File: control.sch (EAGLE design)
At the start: 11 parts, among them J1 1-2328702-0, U2 ESP32-DEVKITC-32D

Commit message: Found wurth typec
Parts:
- added J2: 12401598E4#2A, 12401598E4_2A:12401598E4#2A
- added R1, R2: 2k2, rcl:R-EU_R0805
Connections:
- new net RST: U$1.RST, U2.IO17
- net 3V3: now also R1.2, R2.2
- net SCL: now also R2.1
- net SDA: now also R1.1
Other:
- moved on the sheet: BT2
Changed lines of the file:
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@@
 <part name="C4" library="rcl" library_urn="urn:adsk.eagle:library:334" deviceset="C-EU" device="C1210" package3d_urn="urn:adsk.eagle:package:23619/2" value="100u"/>
 <part name="C5" library="rcl" library_urn="urn:adsk.eagle:library:334" deviceset="C-EU" device="C1210" package3d_urn="urn:adsk.eagle:package:23619/2" value="100u"/>
+<part name="R1" library="rcl" library_urn="urn:adsk.eagle:library:334" deviceset="R-EU_" device="R0805" package3d_urn="urn:adsk.eagle:package:23553/2" value="2k2"/>
+<part name="R2" library="rcl" library_urn="urn:adsk.eagle:library:334" deviceset="R-EU_" device="R0805" package3d_urn="urn:adsk.eagle:package:23553/2" value="2k2"/>
+<part name="J2" library="12401598E4_2A" deviceset="12401598E4#2A" device=""/>
 </parts>
 <sheets>
@@
 <attribute name="VALUE" x="177.8" y="104.14" size="1.778" layer="96"/>
 </instance>
-<instance part="BT2" gate="G$1" x="281.94" y="116.84" smashed="yes" rot="R270">
-<attribute name="NAME" x="285.75" y="120.65" size="1.778" layer="95" rot="R270"/>
-<attribute name="VALUE" x="276.86" y="120.65" size="1.778" layer="96" rot="R270"/>
+<instance part="BT2" gate="G$1" x="281.94" y="114.3" smashed="yes" rot="R270">
+<attribute name="NAME" x="285.75" y="118.11" size="1.778" layer="95" rot="R270"/>
+<attribute name="VALUE" x="276.86" y="118.11" size="1.778" layer="96" rot="R270"/>
 </instance>
 <instance part="C1" gate="G$1" x="215.9" y="121.92" smashed="yes">
@@
 <attribute name="NAME" x="245.364" y="99.441" size="1.778" layer="95"/>
 <attribute name="VALUE" x="245.364" y="94.361" size="1.778" layer="96"/>
+</instance>
+<instance part="R1" gate="G$1" x="284.48" y="137.16" smashed="yes" rot="R90">
+<attribute name="NAME" x="282.9814" y="133.35" size="1.778" layer="95" rot="R90"/>
+<attribute name="VALUE" x="287.782" y="133.35" size="1.778" layer="96" rot="R90"/>
+</instance>
+<instance part="R2" gate="G$1" x="276.86" y="137.16" smashed="yes" rot="R90">
+<attribute name="NAME" x="275.3614" y="133.35" size="1.778" layer="95" rot="R90"/>
+<attribute name="VALUE" x="280.162" y="133.35" size="1.778" layer="96" rot="R90"/>
+</instance>
+<instance part="J2" gate="G$1" x="309.88" y="88.9" smashed="yes">
+<attribute name="NAME" x="302.248009375" y="124.512" size="2.54" layer="95"/>
+<attribute name="VALUE" x="302.24645" y="50.7368" size="2.54" layer="96"/>
 </instance>
 </instances>
@@
 <junction x="261.62" y="116.84"/>
 <pinref part="BT2" gate="G$1" pin="NEG"/>
-<wire x1="261.62" y1="109.22" x2="281.94" y2="109.22" width="0.1524" layer="91"/>
 <junction x="261.62" y="109.22"/>
 <wire x1="246.38" y1="116.84" x2="261.62" y2="116.84" width="0.1524" layer="91"/>
 <junction x="246.38" y="116.84"/>
 <wire x1="215.9" y1="116.84" x2="228.6" y2="116.84" width="0.1524" layer="91"/>
+<wire x1="261.62" y1="109.22" x2="261.62" y2="106.68" width="0.1524" layer="91"/>
+<wire x1="261.62" y1="106.68" x2="281.94" y2="106.68" width="0.1524" layer="91"/>
 </segment>
 <segment>
@@
 <label x="215.9" y="124.46" size="1.778" layer="95"/>
 <pinref part="U$1" gate="G$1" pin="VCC"/>
+<wire x1="215.9" y1="124.46" x2="215.9" y2="142.24" width="0.1524" layer="91"/>
+<junction x="215.9" y="124.46"/>
+<pinref part="R1" gate="G$1" pin="2"/>
+<wire x1="215.9" y1="142.24" x2="276.86" y2="142.24" width="0.1524" layer="91"/>
+<pinref part="R2" gate="G$1" pin="2"/>
+<wire x1="276.86" y1="142.24" x2="284.48" y2="142.24" width="0.1524" layer="91"/>
+<junction x="276.86" y="142.24"/>
 </segment>
 </net>
@@
 <segment>
 <pinref part="U$1" gate="G$1" pin="SCL@1"/>
-<wire x1="261.62" y1="132.08" x2="271.78" y2="132.08" width="0.1524" layer="91"/>
+<wire x1="261.62" y1="132.08" x2="276.86" y2="132.08" width="0.1524" layer="91"/>
 <label x="266.7" y="132.08" size="1.778" layer="95"/>
+<pinref part="R2" gate="G$1" pin="1"/>
 </segment>
 <segment>
@@
 <segment>
 <pinref part="U$1" gate="G$1" pin="SDA"/>
-<wire x1="261.62" y1="124.46" x2="271.78" y2="124.46" width="0.1524" layer="91"/>
+<wire x1="261.62" y1="124.46" x2="284.48" y2="124.46" width="0.1524" layer="91"/>
 <label x="266.7" y="124.46" size="1.778" layer="95"/>
+<wire x1="284.48" y1="124.46" x2="284.48" y2="132.08" width="0.1524" layer="91"/>
+<pinref part="R1" gate="G$1" pin="1"/>
 </segment>
 <segment>
@@
 <segment>
 <pinref part="U$1" gate="G$1" pin="VBAT"/>
-<wire x1="261.62" y1="121.92" x2="276.86" y2="121.92" width="0.1524" layer="91"/>
+<wire x1="261.62" y1="121.92" x2="281.94" y2="121.92" width="0.1524" layer="91"/>
 <pinref part="BT2" gate="G$1" pin="POS"/>
-<label x="279.4" y="124.46" size="1.778" layer="95"/>
-<wire x1="281.94" y1="124.46" x2="276.86" y2="124.46" width="0.1524" layer="91"/>
-<wire x1="276.86" y1="124.46" x2="276.86" y2="121.92" width="0.1524" layer="91"/>
+<label x="279.4" y="121.92" size="1.778" layer="95"/>
 </segment>
 </net>
@@
 <label x="213.36" y="55.88" size="1.778" layer="95"/>
 <pinref part="U2" gate="G$1" pin="IO0"/>
+</segment>
+</net>
+<net name="RST" class="0">
+<segment>
+<pinref part="U$1" gate="G$1" pin="RST"/>
+<wire x1="220.98" y1="119.38" x2="228.6" y2="119.38" width="0.1524" layer="91"/>
+<label x="220.98" y="119.38" size="1.778" layer="95"/>
+</segment>
+<segment>
+<wire x1="213.36" y1="63.5" x2="220.98" y2="63.5" width="0.1524" layer="91"/>
+<label x="213.36" y="63.5" size="1.778" layer="95"/>
+<pinref part="U2" gate="G$1" pin="IO17"/>
 </segment>
 </net>
@@
 packages will not be understood (or retained) with this version.
 </note>
+<note version="8.4" severity="warning">
+Since Version 8.4, EAGLE supports properties for SPICE simulation.
+Probes in schematics and SPICE mapping objects found in parts and library devices
+will not be understood with this version. Update EAGLE to the latest version
+for full support of SPICE simulation.
+</note>
 </compatibility>

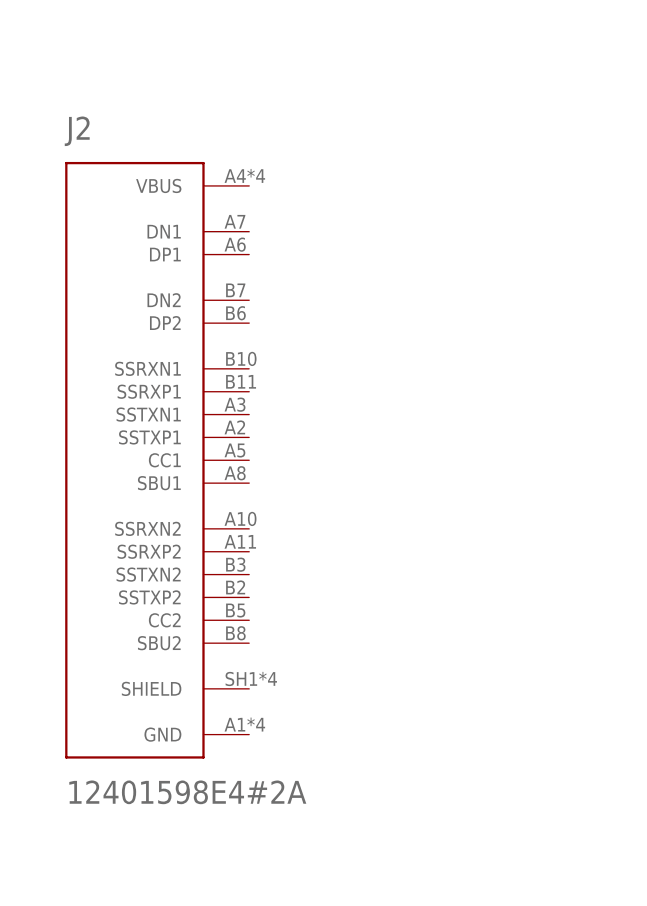
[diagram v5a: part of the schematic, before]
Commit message: started ratsnest, finished usb-c viring
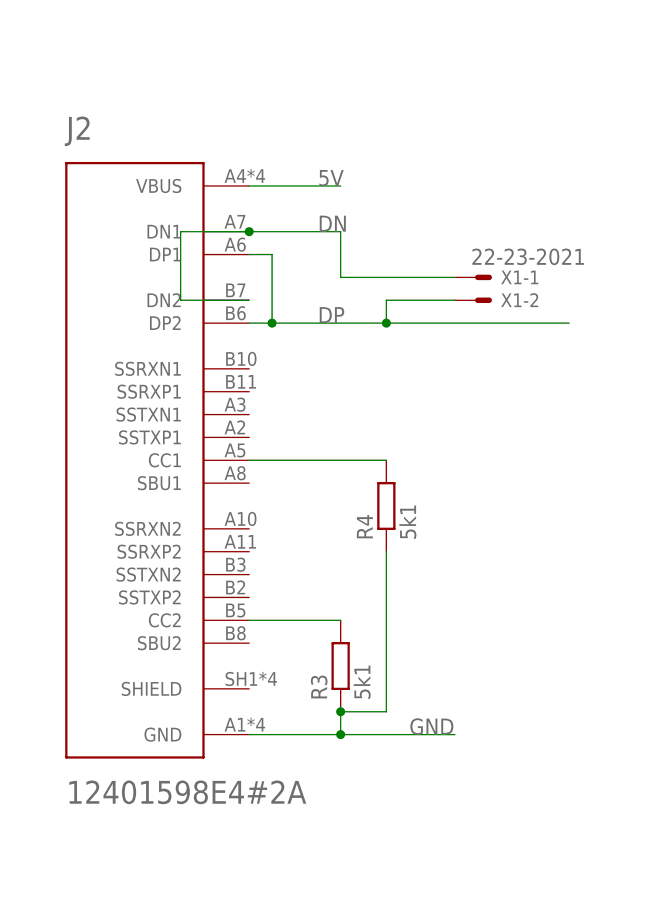
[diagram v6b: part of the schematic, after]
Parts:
- added R3, R4: 5k1, rcl:R-EU_R0805
- added X1: 22-23-2021, con-molex:22-23-2021
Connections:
- new net DN: J2.DN1, J2.DN2, X1-1.S
- new net DP: J2.DP1, J2.DP2, X1-2.S
- new net N$1: J2.CC2, R3.2
- new net N$2: J2.CC1, R4.2
- net 5V: now also J2.VBUS
- net GND: now also J2.GND, R3.1, R4.1
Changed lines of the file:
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@@
 <part name="R2" library="rcl" library_urn="urn:adsk.eagle:library:334" deviceset="R-EU_" device="R0805" package3d_urn="urn:adsk.eagle:package:23553/2" value="2k2"/>
 <part name="J2" library="12401598E4_2A" deviceset="12401598E4#2A" device=""/>
+<part name="R3" library="rcl" library_urn="urn:adsk.eagle:library:334" deviceset="R-EU_" device="R0805" package3d_urn="urn:adsk.eagle:package:23553/2" value="5k1"/>
+<part name="R4" library="rcl" library_urn="urn:adsk.eagle:library:334" deviceset="R-EU_" device="R0805" package3d_urn="urn:adsk.eagle:package:23553/2" value="5k1"/>
+<part name="X1" library="con-molex" library_urn="urn:adsk.eagle:library:165" deviceset="22-23-2021" device="" package3d_urn="urn:adsk.eagle:package:8078633/1"/>
 </parts>
 <sheets>
@@
 <attribute name="VALUE" x="302.24645" y="50.7368" size="2.54" layer="96"/>
 </instance>
+<instance part="R3" gate="G$1" x="332.74" y="66.04" smashed="yes" rot="R90">
+<attribute name="NAME" x="331.2414" y="62.23" size="1.778" layer="95" rot="R90"/>
+<attribute name="VALUE" x="336.042" y="62.23" size="1.778" layer="96" rot="R90"/>
+</instance>
+<instance part="R4" gate="G$1" x="337.82" y="83.82" smashed="yes" rot="R90">
+<attribute name="NAME" x="336.3214" y="80.01" size="1.778" layer="95" rot="R90"/>
+<attribute name="VALUE" x="341.122" y="80.01" size="1.778" layer="96" rot="R90"/>
+</instance>
+<instance part="X1" gate="-1" x="347.98" y="109.22" smashed="yes">
+<attribute name="NAME" x="350.52" y="108.458" size="1.524" layer="95"/>
+<attribute name="VALUE" x="347.218" y="110.617" size="1.778" layer="96"/>
+</instance>
+<instance part="X1" gate="-2" x="347.98" y="106.68" smashed="yes">
+<attribute name="NAME" x="350.52" y="105.918" size="1.524" layer="95"/>
+</instance>
 </instances>
 <busses>
@@
 <pinref part="C2" gate="G$1" pin="1"/>
 <wire x1="279.4" y1="68.58" x2="279.4" y2="63.5" width="0.1524" layer="91"/>
+</segment>
+<segment>
+<wire x1="332.74" y1="119.38" x2="322.58" y2="119.38" width="0.1524" layer="91"/>
+<label x="330.2" y="119.38" size="1.778" layer="95"/>
+<pinref part="J2" gate="G$1" pin="VBUS"/>
 </segment>
 </net>
@@
 <wire x1="266.7" y1="55.88" x2="279.4" y2="55.88" width="0.1524" layer="91"/>
 </segment>
+<segment>
+<label x="340.36" y="58.42" size="1.778" layer="95"/>
+<wire x1="332.74" y1="58.42" x2="345.44" y2="58.42" width="0.1524" layer="91"/>
+<pinref part="R4" gate="G$1" pin="1"/>
+<wire x1="337.82" y1="78.74" x2="337.82" y2="60.96" width="0.1524" layer="91"/>
+<pinref part="R3" gate="G$1" pin="1"/>
+<wire x1="337.82" y1="60.96" x2="332.74" y2="60.96" width="0.1524" layer="91"/>
+<wire x1="332.74" y1="60.96" x2="332.74" y2="58.42" width="0.1524" layer="91"/>
+<junction x="332.74" y="60.96"/>
+<pinref part="J2" gate="G$1" pin="GND"/>
+<wire x1="322.58" y1="58.42" x2="332.74" y2="58.42" width="0.1524" layer="91"/>
+<junction x="332.74" y="58.42"/>
+</segment>
 </net>
 <net name="3V3" class="0">
@@
 </segment>
 </net>
+<net name="N$1" class="0">
+<segment>
+<pinref part="J2" gate="G$1" pin="CC2"/>
+<wire x1="322.58" y1="71.12" x2="332.74" y2="71.12" width="0.1524" layer="91"/>
+<pinref part="R3" gate="G$1" pin="2"/>
+</segment>
+</net>
+<net name="N$2" class="0">
+<segment>
+<pinref part="J2" gate="G$1" pin="CC1"/>
+<wire x1="322.58" y1="88.9" x2="337.82" y2="88.9" width="0.1524" layer="91"/>
+<pinref part="R4" gate="G$1" pin="2"/>
+</segment>
+</net>
+<net name="DN" class="0">
+<segment>
+<pinref part="J2" gate="G$1" pin="DN2"/>
+<wire x1="322.58" y1="106.68" x2="314.96" y2="106.68" width="0.1524" layer="91"/>
+<wire x1="314.96" y1="106.68" x2="314.96" y2="114.3" width="0.1524" layer="91"/>
+<pinref part="J2" gate="G$1" pin="DN1"/>
+<wire x1="314.96" y1="114.3" x2="322.58" y2="114.3" width="0.1524" layer="91"/>
+<junction x="322.58" y="114.3"/>
+<label x="330.2" y="114.3" size="1.778" layer="95"/>
+<wire x1="322.58" y1="114.3" x2="332.74" y2="114.3" width="0.1524" layer="91"/>
+<pinref part="X1" gate="-1" pin="S"/>
+<wire x1="332.74" y1="114.3" x2="332.74" y2="109.22" width="0.1524" layer="91"/>
+<wire x1="332.74" y1="109.22" x2="345.44" y2="109.22" width="0.1524" layer="91"/>
+</segment>
+</net>
+<net name="DP" class="0">
+<segment>
+<pinref part="J2" gate="G$1" pin="DP1"/>
+<wire x1="322.58" y1="111.76" x2="325.12" y2="111.76" width="0.1524" layer="91"/>
+<wire x1="325.12" y1="111.76" x2="325.12" y2="104.14" width="0.1524" layer="91"/>
+<pinref part="J2" gate="G$1" pin="DP2"/>
+<wire x1="325.12" y1="104.14" x2="322.58" y2="104.14" width="0.1524" layer="91"/>
+<junction x="325.12" y="104.14"/>
+<label x="330.2" y="104.14" size="1.778" layer="95"/>
+<wire x1="325.12" y1="104.14" x2="337.82" y2="104.14" width="0.1524" layer="91"/>
+<pinref part="X1" gate="-2" pin="S"/>
+<wire x1="337.82" y1="104.14" x2="358.14" y2="104.14" width="0.1524" layer="91"/>
+<wire x1="345.44" y1="106.68" x2="337.82" y2="106.68" width="0.1524" layer="91"/>
+<wire x1="337.82" y1="106.68" x2="337.82" y2="104.14" width="0.1524" layer="91"/>
+<junction x="337.82" y="104.14"/>
+</segment>
+</net>
